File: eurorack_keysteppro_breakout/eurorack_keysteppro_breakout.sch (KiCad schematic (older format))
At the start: 25 parts, among them J1 AudioJack2_SwitchT, J10 AudioJack2_SwitchT, J11 AudioJack2_SwitchT, J12 AudioJack2_SwitchT, J13 AudioJack2_SwitchT, J14 AudioJack2_SwitchT, J15 AudioJack2_SwitchT, J16 AudioJack2_SwitchT, J17 AudioJack2_SwitchT, J18 Conn_02x08_Odd_Even, J19 AudioJack2_SwitchT, J2 AudioJack2_SwitchT, J20 AudioJack2_SwitchT, J21 AudioJack2_SwitchT, J22 AudioJack2_SwitchT, J23 Conn_02x08_Odd_Even, J24 AudioJack2_SwitchT, J25 AudioJack2_SwitchT, J3 AudioJack2_SwitchT, J4 AudioJack2_SwitchT, J5 AudioJack2_SwitchT, J6 AudioJack2_SwitchT, J7 AudioJack2_SwitchT, J8 AudioJack2_SwitchT, J9 AudioJack2_SwitchT

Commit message: some layout
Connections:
- net GND: no longer J23.11 (Pin_11), J23.13 (Pin_13), J23.15 (Pin_15), J23.7 (Pin_7)
- net ck_in: now also J23.13 (Pin_13); no longer J23.1 (Pin_1)
- net ck_out: now also J23.11 (Pin_11); no longer J23.5 (Pin_5)
- net ck_rst: now also J23.15 (Pin_15); no longer J23.3 (Pin_3)
- net cv1: now also J18.2 (Pin_2); no longer J18.1 (Pin_1)
- net cv2: now also J18.5 (Pin_5); no longer J18.9 (Pin_9)
- net cv3: now also J18.13 (Pin_13); no longer J18.14 (Pin_14)
- net cv4: now also J18.14 (Pin_14); no longer J18.6 (Pin_6)
- net dr1: now also J23.7 (Pin_7); no longer J23.16 (Pin_16)
- net dr2: now also J23.3 (Pin_3); no longer J23.12 (Pin_12)
- net dr3: now also J23.2 (Pin_2); no longer J23.8 (Pin_8)
- net dr4: now also J23.6 (Pin_6); no longer J23.4 (Pin_4)
- net dr5: now also J23.5 (Pin_5); no longer J23.14 (Pin_14)
- net dr6: now also J23.1 (Pin_1); no longer J23.10 (Pin_10)
- net dr7: now also J23.4 (Pin_4); no longer J23.6 (Pin_6)
- net dr8: now also J23.8 (Pin_8); no longer J23.2 (Pin_2)
- net gt1: now also J18.4 (Pin_4); no longer J18.3 (Pin_3)
- net gt2: now also J18.3 (Pin_3); no longer J18.11 (Pin_11)
- net gt3: now also J18.11 (Pin_11); no longer J18.12 (Pin_12)
- net gt4: now also J18.12 (Pin_12); no longer J18.4 (Pin_4)
- net md1: now also J18.6 (Pin_6); no longer J18.5 (Pin_5)
- net md2: now also J18.1 (Pin_1); no longer J18.13 (Pin_13)
- net md3: now also J18.9 (Pin_9); no longer J18.10 (Pin_10)
- net md4: now also J18.10 (Pin_10); no longer J18.2 (Pin_2)
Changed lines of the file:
@@
 Wire Wire Line
 	4450 6050 4700 6050
-Text GLabel 7150 4300 0    50   Input ~ 0
+Text GLabel 7650 4300 2    50   Input ~ 0
 cv1
-Text GLabel 7150 4400 0    50   Input ~ 0
+Text GLabel 7650 4400 2    50   Input ~ 0
 gt1
-Text GLabel 7150 4500 0    50   Input ~ 0
+Text GLabel 7650 4500 2    50   Input ~ 0
 md1
 $Comp
@@
 	1    0    0    -1
 $EndComp
+Text GLabel 7150 4500 0    50   Input ~ 0
+cv2
+Text GLabel 7150 4400 0    50   Input ~ 0
+gt2
+Text GLabel 7150 4300 0    50   Input ~ 0
+md2
+Text GLabel 7150 4900 0    50   Input ~ 0
+cv3
+Text GLabel 7150 4800 0    50   Input ~ 0
+gt3
 Text GLabel 7150 4700 0    50   Input ~ 0
-cv2
-Text GLabel 7150 4800 0    50   Input ~ 0
-gt2
-Text GLabel 7150 4900 0    50   Input ~ 0
-md2
+md3
 Text GLabel 7650 4900 2    50   Input ~ 0
-cv3
+cv4
 Text GLabel 7650 4800 2    50   Input ~ 0
-gt3
+gt4
 Text GLabel 7650 4700 2    50   Input ~ 0
-md3
-Text GLabel 7650 4500 2    50   Input ~ 0
-cv4
-Text GLabel 7650 4400 2    50   Input ~ 0
-gt4
-Text GLabel 7650 4300 2    50   Input ~ 0
 md4
+Text GLabel 8800 4900 0    50   Input ~ 0
+ck_in
+Text GLabel 8800 4800 0    50   Input ~ 0
+ck_out
+Text GLabel 8800 5000 0    50   Input ~ 0
+ck_rst
+Text GLabel 8800 4600 0    50   Input ~ 0
+dr1
+Text GLabel 8800 4400 0    50   Input ~ 0
+dr2
+Text GLabel 9300 4300 2    50   Input ~ 0
+dr3
+Text GLabel 9300 4500 2    50   Input ~ 0
+dr4
+Text GLabel 8800 4500 0    50   Input ~ 0
+dr5
 Text GLabel 8800 4300 0    50   Input ~ 0
-ck_in
-Text GLabel 8800 4500 0    50   Input ~ 0
-ck_out
-Text GLabel 8800 4400 0    50   Input ~ 0
-ck_rst
-Text GLabel 9300 5000 2    50   Input ~ 0
-dr1
-Text GLabel 9300 4800 2    50   Input ~ 0
-dr2
+dr6
+Text GLabel 9300 4400 2    50   Input ~ 0
+dr7
 Text GLabel 9300 4600 2    50   Input ~ 0
-dr3
-Text GLabel 9300 4400 2    50   Input ~ 0
-dr4
-Text GLabel 9300 4900 2    50   Input ~ 0
-dr5
-Text GLabel 9300 4700 2    50   Input ~ 0
-dr6
-Text GLabel 9300 4500 2    50   Input ~ 0
-dr7
-Text GLabel 9300 4300 2    50   Input ~ 0
 dr8
 $Comp
@@
 	8050 5000 8050 5100
 $Comp
-L power:GND #PWR024
-U 1 1 61A7AB11
-P 8700 5100
-F 0 "#PWR024" H 8700 4850 50  0001 C CNN
-F 1 "GND" H 8705 4927 50  0000 C CNN
-F 2 "" H 8700 5100 50  0001 C CNN
-F 3 "" H 8700 5100 50  0001 C CNN
-	1    8700 5100
-	1    0    0    -1
-$EndComp
-$Comp
 L Connector:AudioJack2_SwitchT J2
 U 1 1 61AAFD60
@@
 	1    0    0    -1
 $EndComp
-Wire Wire Line
-	8800 4600 8700 4600
-Wire Wire Line
-	8700 4600 8700 4700
-Wire Wire Line
-	8800 4700 8700 4700
-Connection ~ 8700 4700
-Wire Wire Line
-	8700 4700 8700 4800
-Wire Wire Line
-	8800 4800 8700 4800
-Connection ~ 8700 4800
-Wire Wire Line
-	8700 4800 8700 4900
-Wire Wire Line
-	8800 4900 8700 4900
-Connection ~ 8700 4900
-Wire Wire Line
-	8700 4900 8700 5000
-Wire Wire Line
-	8800 5000 8700 5000
-Connection ~ 8700 5000
-Wire Wire Line
-	8700 5000 8700 5100
+$Comp
+L power:GND #PWR0101
+U 1 1 61BBA297
+P 8350 4800
+F 0 "#PWR0101" H 8350 4550 50  0001 C CNN
+F 1 "GND" H 8355 4627 50  0000 C CNN
+F 2 "" H 8350 4800 50  0001 C CNN
+F 3 "" H 8350 4800 50  0001 C CNN
+	1    8350 4800
+	1    0    0    -1
+$EndComp
+Wire Wire Line
+	8350 4800 8350 4700
+Wire Wire Line
+	8800 4700 8350 4700
 $EndSCHEMATC

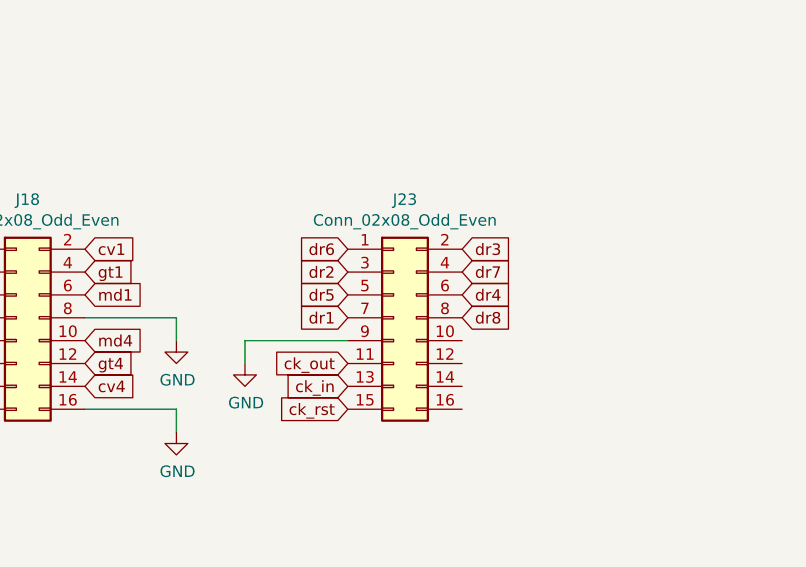
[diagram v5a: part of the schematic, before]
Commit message: reorder pins on clock and trigger header, route the rest of the tracks
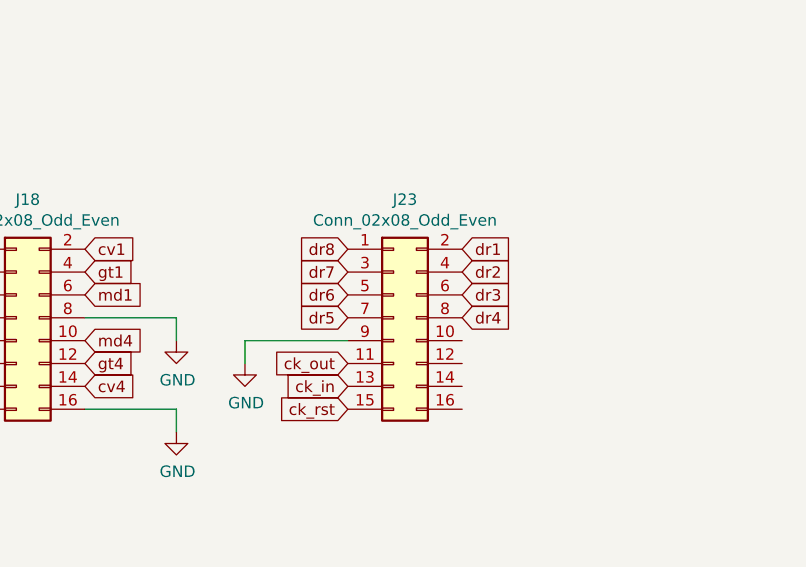
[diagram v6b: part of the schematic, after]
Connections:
- net dr1: now also J23.2 (Pin_2); no longer J23.7 (Pin_7)
- net dr2: now also J23.4 (Pin_4); no longer J23.3 (Pin_3)
- net dr3: now also J23.6 (Pin_6); no longer J23.2 (Pin_2)
- net dr4: now also J23.8 (Pin_8); no longer J23.6 (Pin_6)
- net dr5: now also J23.7 (Pin_7); no longer J23.5 (Pin_5)
- net dr6: now also J23.5 (Pin_5); no longer J23.1 (Pin_1)
- net dr7: now also J23.3 (Pin_3); no longer J23.4 (Pin_4)
- net dr8: now also J23.1 (Pin_1); no longer J23.8 (Pin_8)
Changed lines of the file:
@@
 Text GLabel 8800 5000 0    50   Input ~ 0
 ck_rst
+Text GLabel 9300 4300 2    50   Input ~ 0
+dr1
+Text GLabel 9300 4400 2    50   Input ~ 0
+dr2
+Text GLabel 9300 4500 2    50   Input ~ 0
+dr3
+Text GLabel 9300 4600 2    50   Input ~ 0
+dr4
 Text GLabel 8800 4600 0    50   Input ~ 0
-dr1
+dr5
+Text GLabel 8800 4500 0    50   Input ~ 0
+dr6
 Text GLabel 8800 4400 0    50   Input ~ 0
-dr2
-Text GLabel 9300 4300 2    50   Input ~ 0
-dr3
-Text GLabel 9300 4500 2    50   Input ~ 0
-dr4
-Text GLabel 8800 4500 0    50   Input ~ 0
-dr5
+dr7
 Text GLabel 8800 4300 0    50   Input ~ 0
-dr6
-Text GLabel 9300 4400 2    50   Input ~ 0
-dr7
-Text GLabel 9300 4600 2    50   Input ~ 0
 dr8
 $Comp
